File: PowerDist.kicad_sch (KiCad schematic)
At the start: 21 parts, among them U1 TPS2121RUXR

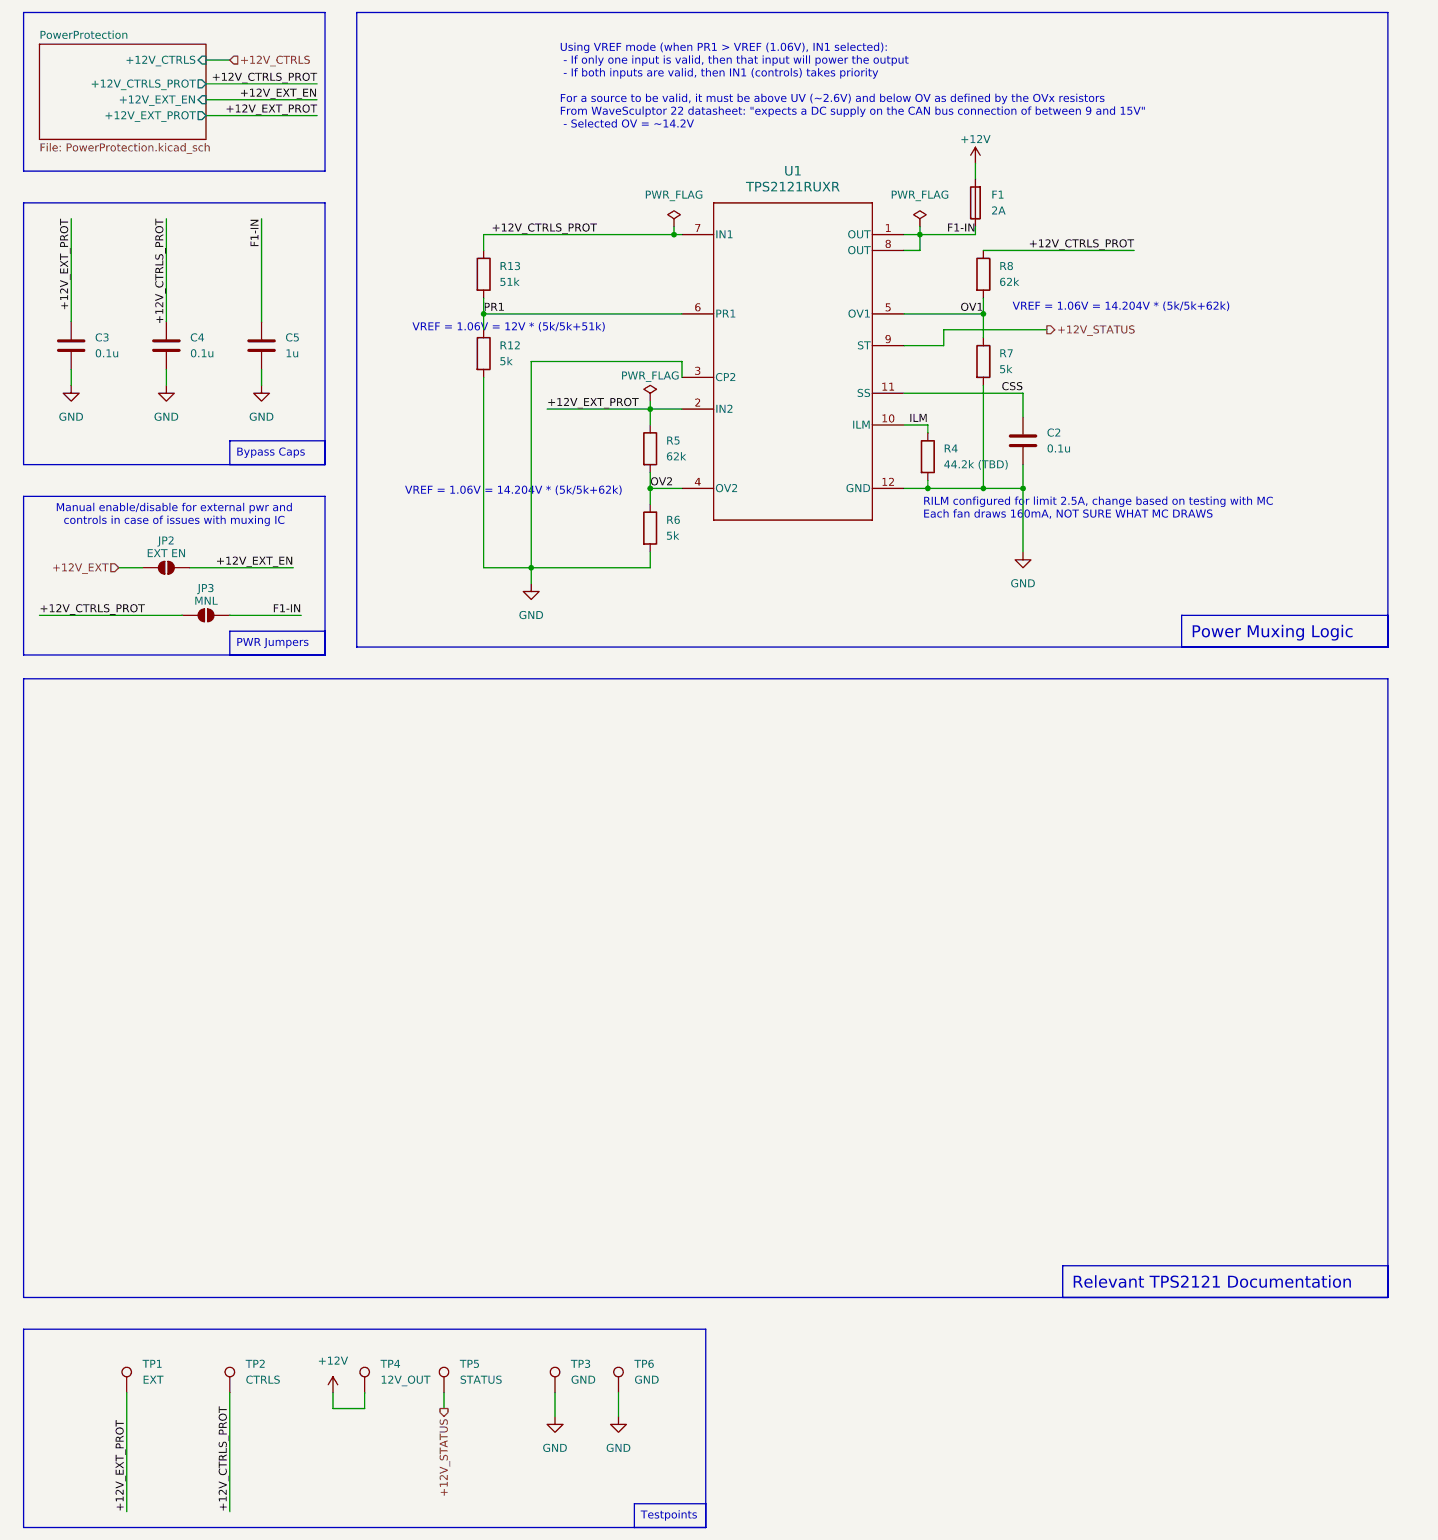
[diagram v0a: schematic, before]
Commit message: modify for PEAK candapter
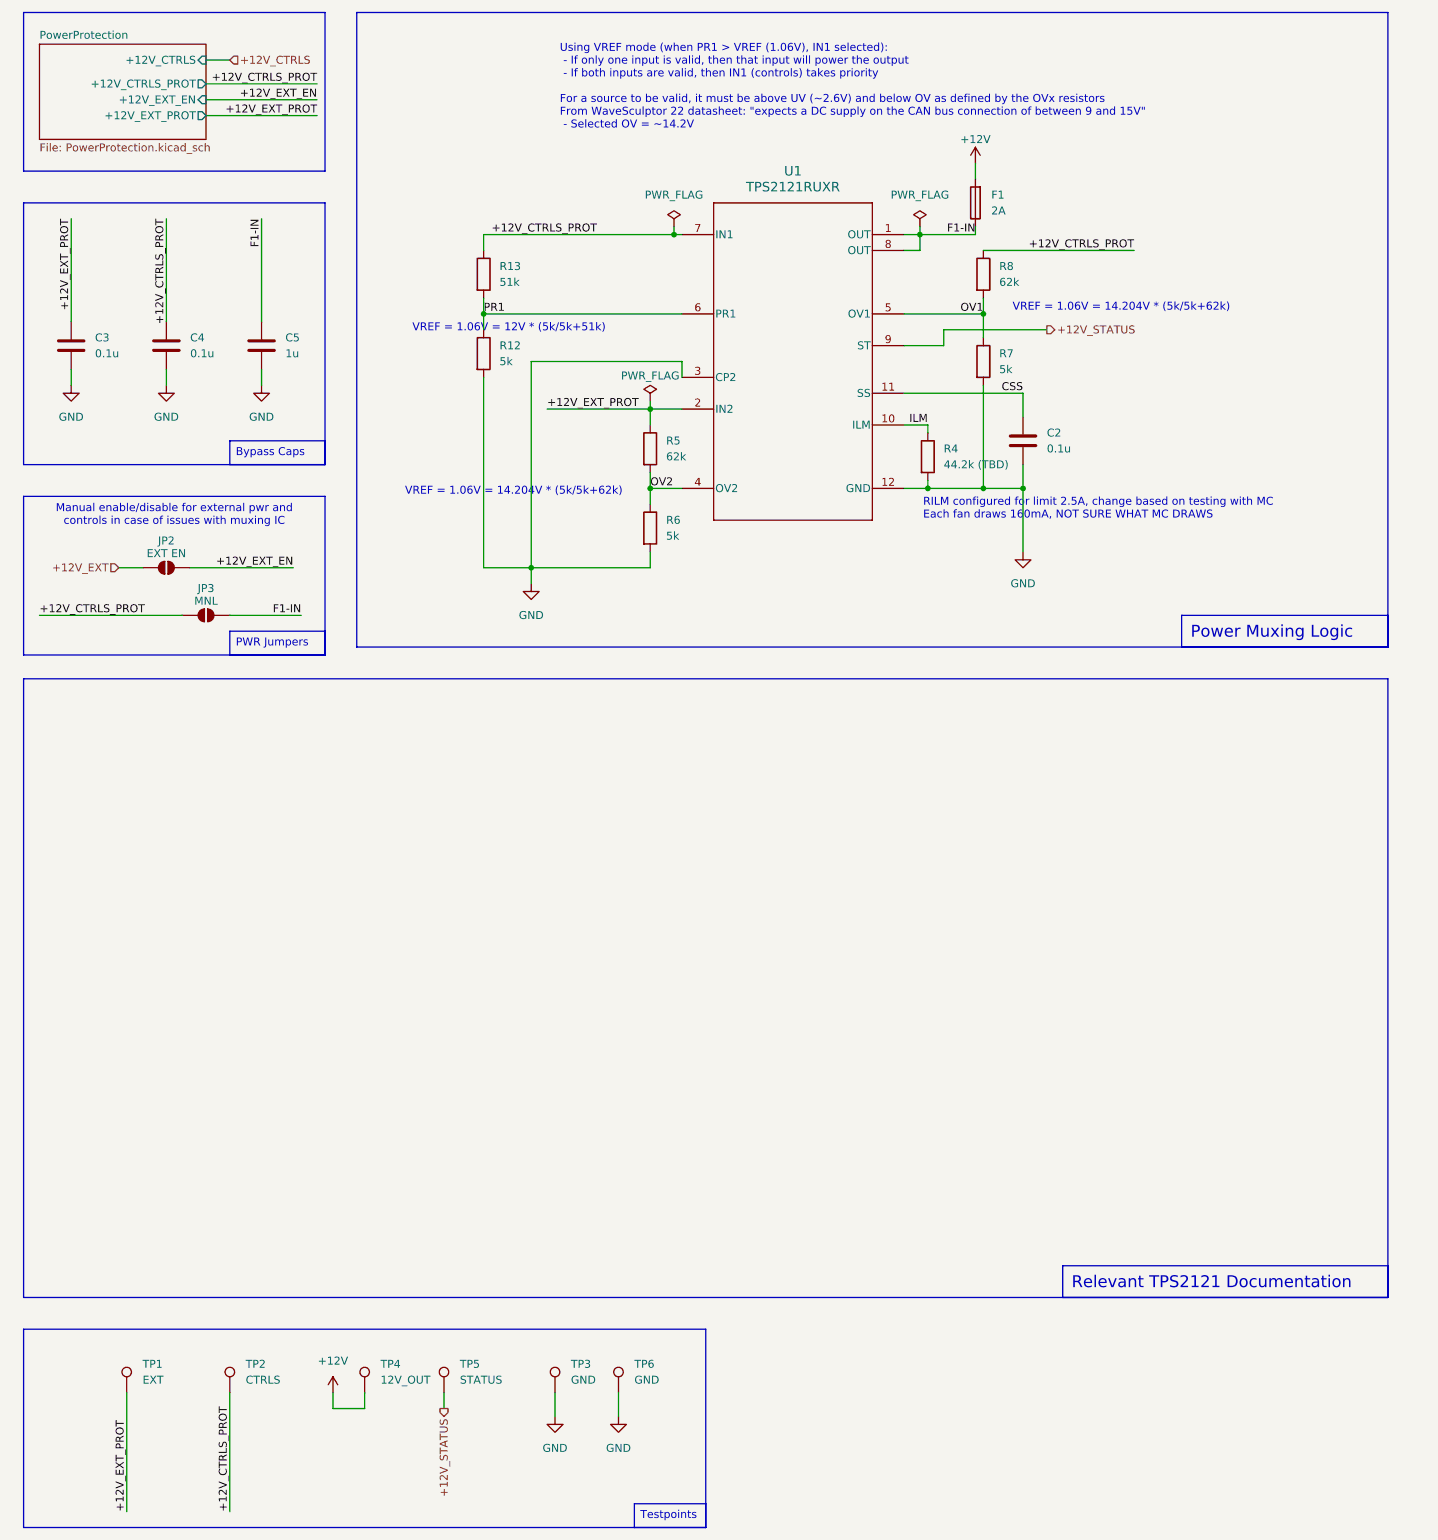
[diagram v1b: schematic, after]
